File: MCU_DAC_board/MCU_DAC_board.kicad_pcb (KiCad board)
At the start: 2 copper layers, 100 x 100 mm, 89 parts, among them J1 Conn_02x04_Odd_Even, J10 Screw_Terminal_01x02, J11 105-0752-001, J2 Conn_02x04_Odd_Even, J3 Conn_02x04_Odd_Even, J4 Conn_02x04_Odd_Even, J5 54-00127, J6 105-0752-001, J7 Screw_Terminal_01x02, J8 Screw_Terminal_01x02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

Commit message: Separated AVDD and PVDD on amplifier board
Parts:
- R35: value 10k -> 2k
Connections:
- R35 pad 2: /DAC_*RST -> /GPIO8
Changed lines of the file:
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@@
 			)
 		)
-		(property "Value" "10k"
+		(property "Value" "2k"
 			(at 0 1.65 0)
 			(layer "F.Fab")
@@
 			(layers "F.Cu" "F.Paste" "F.Mask")
 			(roundrect_rratio 0.208333)
-			(net 63 "/DAC_*RST")
+			(net 70 "/GPIO8")
 			(pintype "passive")
 		)
@@
 			(net 76 "unconnected-(U1-SA1-Pad31)")
 			(pinfunction "SA1")
-			(pintype "unspecified+no_connect")
+			(pintype "unspecified")
 		)
 		(pad "32" smd rect
@@
 			(net 78 "unconnected-(U1-SA2-Pad32)")
 			(pinfunction "SA2")
-			(pintype "unspecified+no_connect")
+			(pintype "unspecified")
 		)
 		(pad "33" smd rect
@@
 			(net 79 "unconnected-(U1-MOSI{slash}ADDR1{slash}SA-Pad42)")
 			(pinfunction "MOSI/ADDR1/SA")
-			(pintype "unspecified+no_connect")
+			(pintype "unspecified")
 		)
 		(pad "43" smd rect
@@
 			(net 80 "unconnected-(U1-*SS{slash}ADDR0{slash}SA-Pad45)")
 			(pinfunction "*SS/ADDR0/SA")
-			(pintype "unspecified+no_connect")
+			(pintype "unspecified")
 		)
 		(pad "46" smd rect
@@
 			(net 74 "unconnected-(U1-SA_MODE-Pad46)")
 			(pinfunction "SA_MODE")
-			(pintype "unspecified+no_connect")
+			(pintype "unspecified")
 		)
 		(pad "47" smd rect

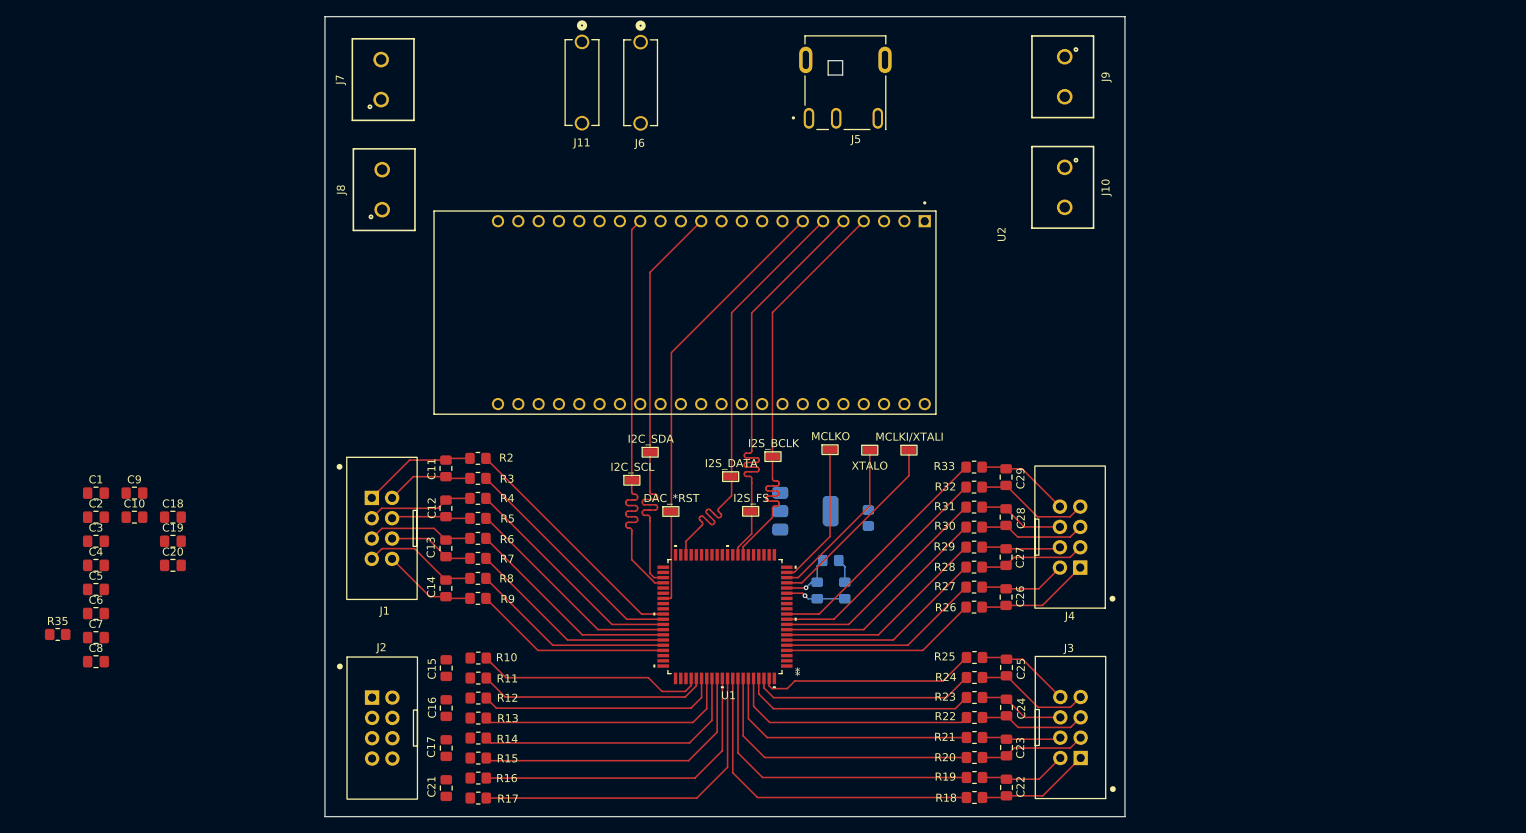
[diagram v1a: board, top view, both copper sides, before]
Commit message: Finished layout for DAC board with 1 MCU
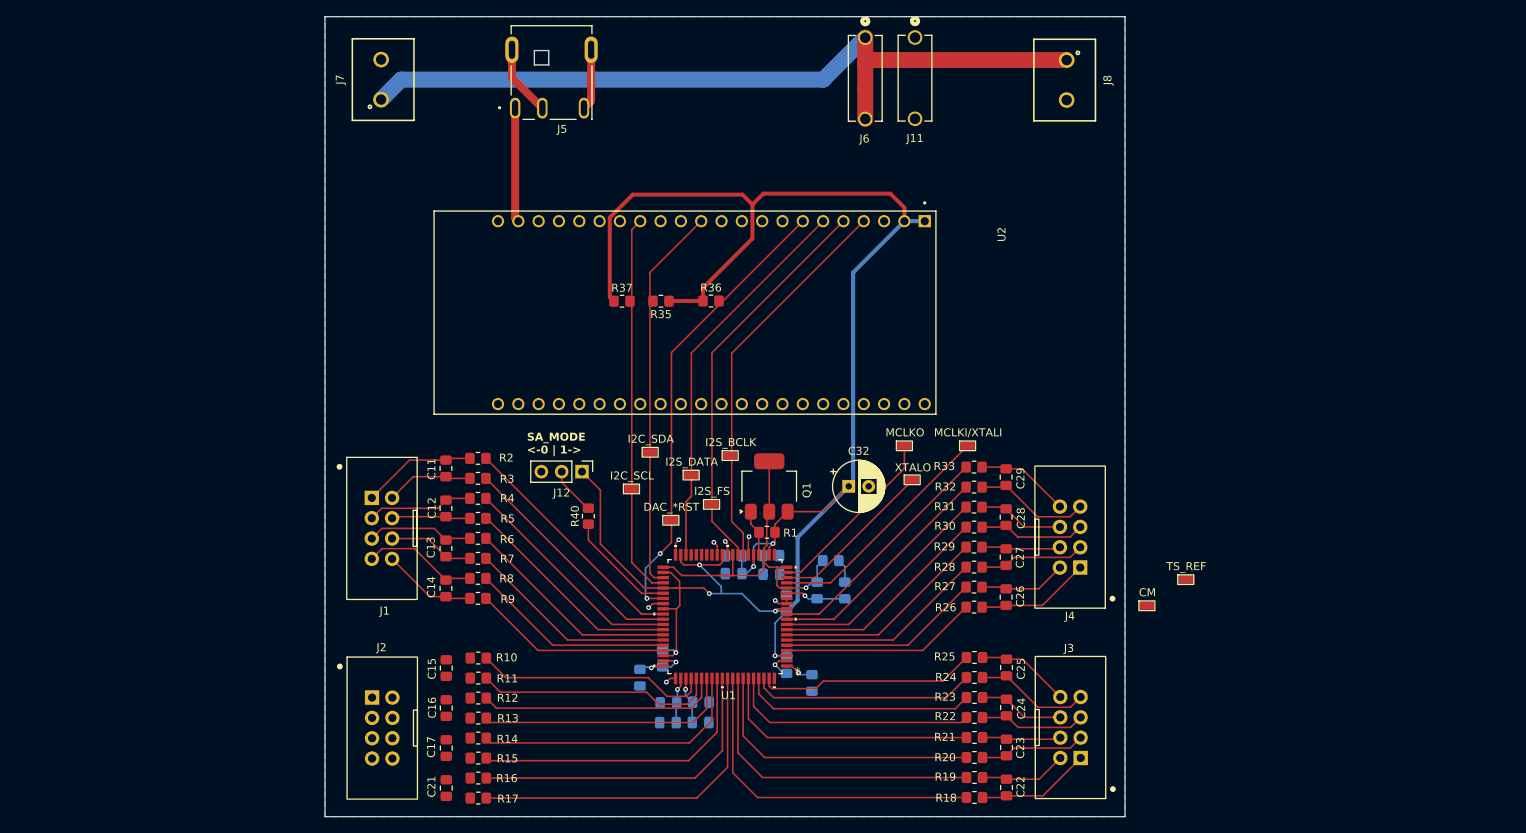
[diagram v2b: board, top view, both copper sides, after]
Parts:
- removed J10, J9: Screw_Terminal_01x02, project_lib:691137710002
- added C32: 100u, Capacitor_THT:CP_Radial_D6.3mm_P2.50mm, F.Cu at (158.5, 117.6)
- added J12: Conn_01x03_Pin, Connector_PinHeader_2.54mm:PinHeader_1x03_P2.54mm_Vertical, F.Cu at (125.2, 115.7)
- added R36: 2k, Resistor_SMD:R_0805_2012Metric_Pad1.20x1.40mm_HandSolder, F.Cu at (141.3, 94.4)
- added R37: 2k, Resistor_SMD:R_0805_2012Metric_Pad1.20x1.40mm_HandSolder, F.Cu at (130.2, 94.4)
- added R40: 2k, Resistor_SMD:R_0805_2012Metric_Pad1.20x1.40mm_HandSolder, F.Cu at (126.0, 121.3)
- added TP10: TS_REF, project_lib:TP_1.8x1mm, F.Cu at (200.7, 129.2)
- added TP11: CM, project_lib:TP_1.8x1mm, F.Cu at (195.8, 132.5)
- C1, C10, C18, C19, C2, C20, C3, C4, C5, C6, C7, C8, C9: moved to B.Cu
- Q1, R1: moved to F.Cu
- moved C9 88.0 mm to (154.0, 142.1), turned to -90 degrees
- moved C1 87.4 mm to (150.8, 132.2), turned to 90 degrees
- moved J8 86.6 mm to (185.8, 66.8), turned to -90 degrees
- moved C8 86.3 mm to (150.8, 139.9), turned to 90 degrees
- moved R35 86.1 mm to (135.1, 94.4), turned to 180 degrees
- moved C6 76.8 mm to (140.0, 147.1)
- moved C7 76.0 mm to (140.1, 144.6)
- moved C10 75.2 mm to (144.2, 128.5), turned to 180 degrees
- moved C18 75.0 mm to (148.9, 126.2)
- moved C20 74.8 mm to (148.9, 128.6)
- moved C4 73.6 mm to (136.0, 144.6), turned to 180 degrees
- moved C5 73.4 mm to (135.9, 147.1), turned to 180 degrees
- moved C3 72.3 mm to (135.3, 139.1), turned to 90 degrees
- moved C2 70.9 mm to (132.5, 141.5), turned to -90 degrees
- moved C19 70.1 mm to (144.2, 126.3), turned to 180 degrees
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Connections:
- Q1 pad 1: +3V3 -> +2V5
- Q1 pad 3: +2V5 -> +3V3
- U1 pad 31: unconnected-(U1-SA1-Pad31) -> +3V3
- U1 pad 32: unconnected-(U1-SA2-Pad32) -> GND
- U1 pad 42: unconnected-(U1-MOSI/ADDR1/SA-Pad42) -> +3V3
- U1 pad 45: unconnected-(U1-*SS/ADDR0/SA-Pad45) -> +3V3
- U1 pad 46: unconnected-(U1-SA_MODE-Pad46) -> /SA_MODE
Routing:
- net +3V3: track 0.00 -> 231.5 mm, vias 0 -> 7
- net +24V: track 0.00 -> 99.3 mm
- net +2V5: track 7.09 -> 48.5 mm
- net GND: track 0.00 -> 30.1 mm, vias 0 -> 7
- net +5V: track 0.00 -> 14.3 mm
- net /SA_MODE: track 0.00 -> 14.1 mm
- net /GPIO9: track 54.8 -> 48.1 mm
- net /GPIO8: track 54.8 -> 48.6 mm
- net /GPIO6: track 55.0 -> 48.8 mm
- net Net-(J12-Pin_2): track 0.00 -> 6.00 mm
- net Net-(U1-TS_REF): track 0.00 -> 5.91 mm, vias 0 -> 1
- net /VDRIVE: track 0.00 -> 5.83 mm
- net Net-(U1-CM): track 0.00 -> 5.76 mm, vias 0 -> 1
- net /GPIO4: track 54.8 -> 49.1 mm
- net /MCLKI/XTALI: track 24.0 -> 29.7 mm
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- added copper zone on B.Cu, net GND
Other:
- board text added: "SA_MODE <-0 | 1->"

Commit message: did a thing
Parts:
- added U3: ESP32-S3-DEVKITC-1-N8R2, project_lib:XCVR_ESP32-S3-DEVKITC-1-N8R2, F.Cu at (167.1, 118.9)
- moved C2 91.3 mm to (55.2, 92.9)
- moved C9 91.3 mm to (76.7, 93.5)
- moved C1 91.3 mm to (73.5, 83.6)
- moved C10 91.3 mm to (66.9, 79.9)
- moved C18 91.3 mm to (71.6, 77.6)
- moved C19 91.3 mm to (66.9, 77.6)
- moved C3 91.3 mm to (58.0, 90.5)
- moved C30 91.3 mm to (80.8, 82.0)
- moved C31 91.3 mm to (77.3, 82.0)
- moved C6 91.3 mm to (62.8, 98.5)
- moved C7 91.3 mm to (62.8, 95.9)
- moved C8 91.3 mm to (73.5, 91.3)
- moved R34 91.3 mm to (79.0, 78.2)
- moved C20 91.3 mm to (71.6, 79.9)
- moved C4 91.3 mm to (58.7, 96.0)
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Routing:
- net +3V3: track 231.5 -> 0.00 mm, vias 7 -> 0
- net +24V: track 99.3 -> 0.00 mm
- net /DAC_*RST: track 57.4 -> 0.00 mm, vias 2 -> 0
- net /GPIO5: track 49.9 -> 0.00 mm
- net /GPIO4: track 49.1 -> 0.00 mm
- net /GPIO6: track 48.8 -> 0.00 mm
- net /GPIO8: track 48.6 -> 0.00 mm
- net +2V5: track 48.5 -> 0.00 mm, vias 1 -> 0
- net /GPIO9: track 48.1 -> 0.00 mm
- net /DAC8N: track 42.9 -> 0.00 mm
- net /DAC9P: track 42.3 -> 0.00 mm
- net /DAC8P: track 40.0 -> 0.00 mm
- net /DAC9N: track 39.1 -> 0.00 mm
- net /DAC7N: track 37.2 -> 0.00 mm
- net /DAC10P: track 36.2 -> 0.00 mm
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
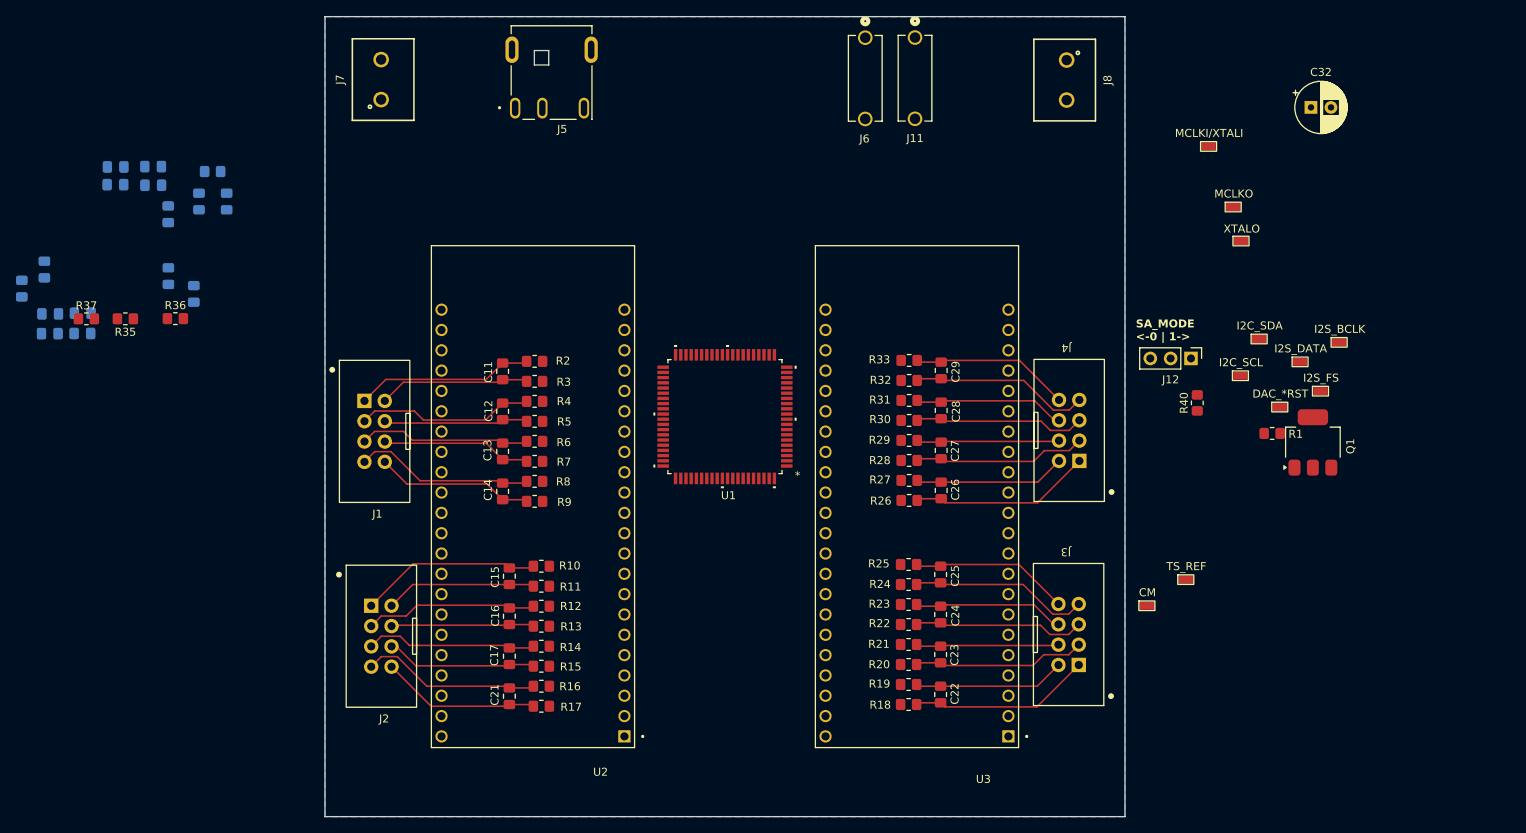
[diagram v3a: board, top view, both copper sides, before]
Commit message: Updated ribbon connector on amp board
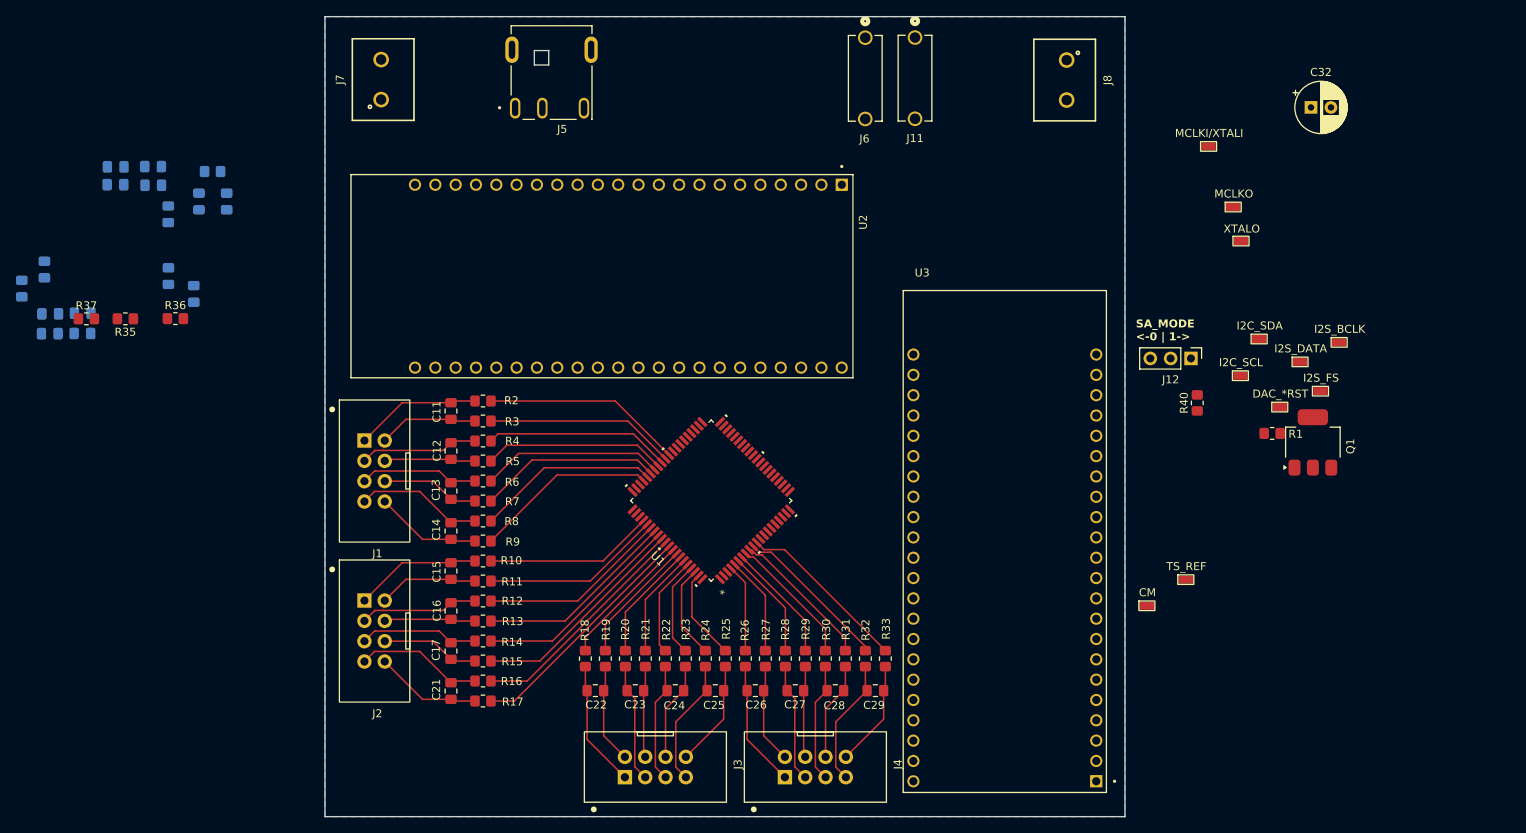
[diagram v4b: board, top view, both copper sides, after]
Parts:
- moved J3 54.2 mm to (134.4, 152.7), turned to 90 degrees
- moved J4 52.7 mm to (154.4, 152.7), turned to 90 degrees
- moved C22 43.2 mm to (126.9, 143.1), turned to 0 degrees
- moved C29 40.9 mm to (161.9, 143.1), turned to 0 degrees
- moved R18 40.8 mm to (125.6, 139.1), turned to -90 degrees
- moved C23 38.4 mm to (131.9, 143.1), turned to 0 degrees
- moved R19 38.0 mm to (128.1, 139.1), turned to -90 degrees
- moved C28 37.4 mm to (156.9, 143.1), turned to 0 degrees
- moved R33 37.4 mm to (163.1, 139.1), turned to -90 degrees
- moved R20 35.4 mm to (130.6, 139.1), turned to -90 degrees
- moved R32 35.2 mm to (160.6, 139.1), turned to -90 degrees
- moved C27 35.1 mm to (151.9, 143.1), turned to 0 degrees
- moved C24 34.5 mm to (136.9, 143.1), turned to 0 degrees
- moved C26 34.1 mm to (146.9, 143.1), turned to 0 degrees
- moved R31 33.2 mm to (158.1, 139.1), turned to -90 degrees
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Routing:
- net /DAC8N: track 0.00 -> 30.3 mm
- net /DAC8P: track 0.00 -> 29.0 mm
- net /DAC7N: track 0.00 -> 27.7 mm
- net /DAC7P: track 0.00 -> 26.4 mm
- net /DAC1P: track 0.00 -> 25.1 mm
- net /DAC6N: track 0.00 -> 25.1 mm
- net /DAC6P: track 0.00 -> 23.8 mm
- net /DAC1N: track 0.00 -> 23.8 mm
- net /DAC2P: track 0.00 -> 23.2 mm
- net /DAC3N: track 0.00 -> 22.8 mm
- net /DAC4N: track 0.00 -> 22.8 mm
- net /DAC4P: track 0.00 -> 22.8 mm
- net /DAC2N: track 0.11 -> 22.8 mm
- net /DAC5N: track 0.00 -> 22.5 mm
- net /DAC3P: track 0.28 -> 22.7 mm
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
